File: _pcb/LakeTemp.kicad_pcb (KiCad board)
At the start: 2 copper layers, 98 x 70 mm, 50 parts, among them J1 Conn_01x06_Male, J2 Conn_01x03_Male, J3 Conn_01x02_Female, J4 Conn_01x14_Female, J5 Conn_01x04_Male, J6 Conn_01x06_Male, J7 Conn_01x02_Female, J8 Conn_01x03_Female, J9 Conn_01x02_Female, Q1 S8050, SW1 RESET, SW2 FLASH, U1 PCF8574, U2 ICL7660, U3 NCP1117-3.3_SOT223, U4 ESP-12E, U5 DS18B20

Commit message: Update PCB
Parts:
- removed ADR-A0: SolderJumper_2_Open, Jumper:SolderJumper-2_P1.3mm_Open_TrianglePad1.0x1.5mm
- added ADR-A3: SolderJumper_2_Open, Jumper:SolderJumper-2_P1.3mm_Open_TrianglePad1.0x1.5mm, F.Cu at (188.1, 84.2)
- added C6: 1000uF, Capacitor_SMD:CP_Elec_10x10.5, F.Cu at (154.5, 90.0)
- added D4: PWR 3.3V, LED_SMD:LED_0805_2012Metric_Pad1.15x1.40mm_HandSolder, F.Cu at (181.0, 111.3)
- added D5: WS2812B, LED_SMD:LED_WS2812B_PLCC4_5.0x5.0mm_P3.2mm, B.Cu at (120.6, 55.2)
- added J10: Conn_01x03_Male, Connector_JST:JST_PH_B3B-PH-K_1x03_P2.00mm_Vertical, F.Cu at (114.0, 67.0)
- added JP2: SolderJumper_3_Open, Connector_PinHeader_2.54mm:PinHeader_1x03_P2.54mm_Vertical, F.Cu at (113.5, 81.5)
- added R15: 4,7k, Resistor_SMD:R_0805_2012Metric_Pad1.20x1.40mm_HandSolder, F.Cu at (127.5, 74.8)
- added R16: 10k, Resistor_SMD:R_0805_2012Metric_Pad1.20x1.40mm_HandSolder, F.Cu at (127.6, 65.7)
- C1, C2, C3, C4: value 10uF 50V -> 10uF
- D1: value WS2812B -> PWR 5V; footprint LED_SMD:LED_WS2812B_PLCC4_5.0x5.0mm_P3.2mm -> LED_SMD:LED_0805_2012Metric_Pad1.15x1.40mm_HandSolder; moved to F.Cu
- D2: value LED -> PWR 3.3V
- D3: value LED -> PWR 5V
- J1: value Conn_01x06_Male -> Conn_01x02_Female; footprint Connector_JST:JST_PH_S6B-PH-K_1x06_P2.00mm_Horizontal -> TerminalBlock_Phoenix:TerminalBlock_Phoenix_MKDS-1,5-2-5.08_1x02_P5.08mm_Horizontal
- J2: value Conn_01x03_Male -> Conn_01x06_Male; footprint Connector_JST:JST_PH_B3B-PH-K_1x03_P2.00mm_Vertical -> Connector_JST:JST_PH_S6B-PH-K_1x06_P2.00mm_Horizontal
- J3: value Conn_01x02_Female -> Conn_01x06_Male; footprint Connector_JST:JST_PH_B2B-PH-K_1x02_P2.00mm_Vertical -> Connector_JST:JST_PH_B6B-PH-K_1x06_P2.00mm_Vertical
- J4: value Conn_01x14_Female -> Conn_01x03_Female; footprint Connector_PinHeader_2.54mm:PinHeader_1x14_P2.54mm_Vertical -> TerminalBlock_Phoenix:TerminalBlock_Phoenix_MKDS-1,5-3-5.08_1x03_P5.08mm_Horizontal; moved to F.Cu
- J5: value Conn_01x04_Male -> Conn_01x02_Female; footprint Connector_PinHeader_2.54mm:PinHeader_1x04_P2.54mm_Vertical -> TerminalBlock_Phoenix:TerminalBlock_Phoenix_MKDS-1,5-2-5.08_1x02_P5.08mm_Horizontal
- J6: value Conn_01x06_Male -> Conn_01x02_Female; footprint Connector_JST:JST_PH_B6B-PH-K_1x06_P2.00mm_Vertical -> Connector_JST:JST_PH_B2B-PH-K_1x02_P2.00mm_Vertical
- J7: value Conn_01x02_Female -> Conn_01x04_Male; footprint TerminalBlock_Phoenix:TerminalBlock_Phoenix_MKDS-1,5-2-5.08_1x02_P5.08mm_Horizontal -> Connector_PinHeader_2.54mm:PinHeader_1x04_P2.54mm_Vertical
- J8: value Conn_01x03_Female -> Conn_01x14_Female; footprint TerminalBlock_Phoenix:TerminalBlock_Phoenix_MKDS-1,5-3-5.08_1x03_P5.08mm_Horizontal -> Connector_PinHeader_2.54mm:PinHeader_1x14_P2.54mm_Vertical; moved to B.Cu
- J9: value Conn_01x02_Female -> Conn_01x04_Female; footprint TerminalBlock_Phoenix:TerminalBlock_Phoenix_MKDS-1,5-2-5.08_1x02_P5.08mm_Horizontal -> Connector_PinSocket_2.54mm:PinSocket_1x04_P2.54mm_Vertical
- JP1: footprint Jumper:SolderJumper-3_P2.0mm_Open_TrianglePad1.0x1.5mm -> Jumper:SolderJumper-3_P1.3mm_Bridged12_Pad1.0x1.5mm
- Q1: footprint Package_TO_SOT_SMD:SOT-23_Handsoldering -> Package_TO_SOT_THT:TO-92_Inline
- R1, R3: value 4,7k -> 150
- R11: value R_PHOTO -> 4,7k; footprint OptoDevice:R_LDR_5.1x4.3mm_P3.4mm_Vertical -> Resistor_SMD:R_0805_2012Metric_Pad1.20x1.40mm_HandSolder; moved to F.Cu
- R12: value R -> 10k
- R13: value R -> 4,7k
- R14: value R -> GL5528; footprint Resistor_SMD:R_0805_2012Metric_Pad1.20x1.40mm_HandSolder -> OptoDevice:R_LDR_5.1x4.3mm_P3.4mm_Vertical; moved to B.Cu
- R2, R4: value 4,7k -> 68
- R8: value 10k -> 4,7k
- SW1, SW2: footprint Button_Switch_SMD:SW_Push_1P1T_NO_6x6mm_H9.5mm -> Button_Switch_THT:SW_PUSH_6mm_H5mm
- U1: value PCF8574 -> NCP1117-3.3_SOT223; footprint Package_SO:SO-16_5.3x10.2mm_P1.27mm -> Package_TO_SOT_SMD:SOT-223-3_TabPin2
- U3: value NCP1117-3.3_SOT223 -> PCF8574; footprint Package_TO_SOT_SMD:SOT-223-3_TabPin2 -> Package_SO:SO-16_5.3x10.2mm_P1.27mm
- moved R14 93.3 mm to (110.5, 55.1)
- moved J9 82.9 mm to (124.1, 96.8), turned to 180 degrees
- moved C4 81.5 mm to (193.0, 68.2), turned to 180 degrees
- moved J8 81.1 mm to (194.5, 61.8), turned to 90 degrees
- moved C3 79.1 mm to (193.0, 66.0)
- moved J6 78.0 mm to (114.0, 76.0), turned to 90 degrees
- moved R13 67.1 mm to (127.5, 72.5), turned to 180 degrees
- moved J7 63.9 mm to (135.7, 84.3), turned to 90 degrees
- moved R11 58.9 mm to (176.5, 86.5)
- moved J4 58.7 mm to (162.4, 124.5), turned to 0 degrees
- moved R3 55.8 mm to (181.1, 106.7)
- moved R8 47.6 mm to (151.3, 68.0), turned to 180 degrees
- moved J2 47.2 mm to (165.0, 94.1), turned to 0 degrees
- moved J3 47.0 mm to (162.5, 109.3), turned to 0 degrees
- moved SW2 46.9 mm to (171.3, 66.7), turned to 270 degrees
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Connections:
- ADR-A1 pad 1: PCF_A1 -> PCF_A0
- ADR-A2 pad 1: PCF_A2 -> PCF_A1
- C1 pad 1: GND -> +5V
- C1 pad 2: Net-(C1-Pad2) -> GND
- C2 pad 1: Net-(C2-Pad1) -> +3V3
- C2 pad 2: Net-(C2-Pad2) -> GND
- C3 pad 1: +5V -> Net-(C3-Pad1)
- C3 pad 2: GND -> Net-(C3-Pad2)
- C4 pad 1: +3V3 -> Net-(C4-Pad1)
- D1 pad 1: +5V -> GND
- D1 pad 2: (no net) -> Net-(D1-Pad2)
- J1 pad 2: +5V -> Net-(J1-Pad2)
- J2 pad 2: +3V3 -> +5V
- J2 pad 3: TOUCH_IO -> +3V3
- J3 pad 1: +5V -> GND
- J3 pad 2: Net-(J3-Pad2) -> Net-(J1-Pad2)
- J4 pad 1: GND -> Net-(J3-Pad4)
- J4 pad 2: +5V -> Net-(J3-Pad5)
- J4 pad 3: LCD_CONTRAST -> GND
- J5 pad 1: ESP_TX -> Net-(J3-Pad3)
- J5 pad 2: ESP_RX -> Net-(J3-Pad6)
- J6 pad 1: Net-(J6-Pad1) -> +5V
- J7 pad 1: Net-(J6-Pad1) -> ESP_TX
- J7 pad 2: Net-(J6-Pad2) -> ESP_RX
- J8 pad 1: Net-(J6-Pad4) -> GND
- J8 pad 2: Net-(J6-Pad5) -> +5V
- J8 pad 3: GND -> LCD_CONTRAST
- J9 pad 1: Net-(J6-Pad3) -> +3V3
- J9 pad 2: Net-(J6-Pad6) -> GND
- Q1 pad 3: Net-(J3-Pad2) -> Net-(JP2-Pad3)
- R1 pad 1: +3V3 -> +5V
- R1 pad 2: SDA -> Net-(D1-Pad2)
- R11 pad 1: +3V3 -> ONEWIRE_PWR
- R11 pad 2: LDR -> ONEWIRE_BUS
- R12 pad 1: LDR -> GND
- R12 pad 2: GND -> Net-(R12-Pad2)
- R13 pad 1: Net-(J6-Pad2) -> WATER_LEVEL
- R13 pad 2: Net-(D2-Pad2) -> GND
- R14 pad 1: Net-(J6-Pad3) -> +3V3
- R14 pad 2: Net-(D3-Pad2) -> LDR
- R2 pad 2: SCL -> Net-(D2-Pad2)
- R3 pad 1: +5V -> Net-(J1-Pad2)
- R3 pad 2: LCD_LED -> Net-(D3-Pad2)
- R4 pad 1: +3V3 -> Net-(J3-Pad3)
- R4 pad 2: ONEWIRE_BUS -> Net-(D4-Pad2)
- R8 pad 1: GND -> +3V3
- R8 pad 2: Net-(R8-Pad2) -> SDA
- R9 pad 1: WATER_LEVEL -> +3V3
- R9 pad 2: GND -> SCL
- RV1 pad 1: Net-(C1-Pad2) -> Net-(C4-Pad1)
- U1 pad 1: PCF_A0 -> GND
- U1 pad 2: PCF_A1 -> +3V3
- U1 pad 3: PCF_A2 -> +5V
- U2 pad 1: (no net) -> Net-(U2-Pad1)
- U2 pad 2: Net-(C2-Pad1) -> Net-(C3-Pad1)
- U2 pad 4: Net-(C2-Pad2) -> Net-(C3-Pad2)
- U2 pad 5: Net-(C1-Pad2) -> Net-(C4-Pad1)
- U2 pad 6: (no net) -> Net-(U2-Pad6)
- U2 pad 7: (no net) -> Net-(U2-Pad7)
- U3 pad 1: GND -> PCF_A0
- U3 pad 2: +3V3 -> PCF_A1
- U3 pad 3: +5V -> PCF_A2
- U4 pad 10: (no net) -> Net-(U4-Pad10)
- U4 pad 11: (no net) -> Net-(U4-Pad11)
- U4 pad 12: (no net) -> Net-(U4-Pad12)
- U4 pad 13: (no net) -> Net-(U4-Pad13)
- U4 pad 14: (no net) -> Net-(U4-Pad14)
- U4 pad 16: Net-(R8-Pad2) -> Net-(R12-Pad2)
- U4 pad 9: (no net) -> Net-(U4-Pad9)
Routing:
- net Net-(J3-Pad3): track 0.00 -> 42.8 mm
- net Net-(J1-Pad2): track 0.00 -> 34.8 mm
- net Net-(J3-Pad6): track 0.00 -> 22.3 mm
- net Net-(J3-Pad4): track 0.00 -> 17.7 mm
- net Net-(J3-Pad5): track 0.00 -> 16.5 mm
- net Net-(D3-Pad2): track 0.00 -> 2.29 mm
- net Net-(D4-Pad2): track 0.00 -> 2.29 mm
- net GND: vias 0 -> 1
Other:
- board size 98 x 70 mm -> 90 x 82 mm
- board text added: "1W+"
- board text added: "1WD"
- board text added: "3.3V"
- board text added: "3.3V 1W PWR 5V"
- board text added: "3.3V OK"
- board text added: "5V"
- board text added: "5V OK"
- board text added: "ADR1"
- board text added: "ADR2"
- board text added: "ADR3"
- board text added: "BME280"
- board text added: "CONNECTOR PCB"
- board text added: "DATA"
- board text added: "ESP TXD/RXD"
- board text added: "FIX | Q1 LED PWR"
- board text added: "FLASH"
- board text added: "GND"
- board text added: "IO"
- board text added: "JLCJLCJLCJLC"
- board text added: "LCD LED"
- board text added: "MAIN PCB"
- board text added: "ONEWIRE"
- board text added: "PWR IN"
- board text added: "RESET"
- board text added: "RX"
- board text added: "STATUS"
- board text added: "TOUCH BTN"
- board text added: "TX"
- board text added: "VCC"
- board text added: "WATER LVL"
- board text added: "WTR"

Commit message: Finished PCB v1.0
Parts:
- added REF**: KiCad-Logo2_5mm_SilkScreen, Symbol:KiCad-Logo2_5mm_SilkScreen, B.Cu at (173.3, 78.3)
- added REF**: KiCad-Logo2_5mm_SilkScreen, Symbol:KiCad-Logo2_5mm_SilkScreen, B.Cu at (167.3, 115.3)
- moved C3 3.18 mm to (193.0, 69.2)
- moved C2 2.75 mm to (176.5, 84.2)
- moved C1 2.00 mm to (176.5, 82.0)
- moved J7 1.89 mm to (135.7, 86.2)
- moved D1 1.78 mm to (138.7, 94.8)
- moved D2 1.78 mm to (138.8, 97.3)
- moved R1 1.78 mm to (142.8, 94.8)
- moved R2 1.78 mm to (142.8, 97.3)
- moved C4 1.61 mm to (193.0, 66.6), turned to 0 degrees
- moved R9 0.90 mm to (151.4, 64.8)
- moved R16 0.89 mm to (127.6, 64.8)
- moved U1 0.69 mm to (169.3, 84.2), turned to 180 degrees
- moved R5 0.63 mm to (127.6, 67.4)
- moved R8 0.62 mm to (151.4, 67.4)
- moved R3 0.51 mm to (181.1, 106.2)
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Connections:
- D3 pad 1: GND -> GND1
- D4 pad 1: GND -> GND1
- J1 pad 1: GND -> GND1
- J3 pad 1: GND -> GND1
- J4 pad 3: GND -> GND1
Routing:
- net +3V3: track 0.00 -> 219.5 mm, vias 0 -> 1
- net +5V: track 0.00 -> 190.7 mm, vias 0 -> 6
- net SCL: track 0.00 -> 82.3 mm, vias 0 -> 4
- net SDA: track 0.00 -> 78.6 mm, vias 0 -> 6
- net ONEWIRE_BUS: track 0.00 -> 75.5 mm, vias 0 -> 4
- net LCD_LED: track 0.00 -> 71.2 mm, vias 0 -> 4
- net WATER_LEVEL: track 0.00 -> 69.1 mm, vias 0 -> 2
- net Net-(R5-Pad1): track 0.00 -> 46.9 mm, vias 0 -> 2
- net Net-(R7-Pad1): track 0.00 -> 39.9 mm, vias 0 -> 1
- net ONEWIRE_PWR: track 0.00 -> 34.6 mm
- net ESP_TX: track 0.00 -> 30.2 mm, vias 0 -> 1
- net ESP_RX: track 0.00 -> 27.5 mm, vias 0 -> 1
- net LCD_CONTRAST: track 0.00 -> 26.8 mm
- net TOUCH_IO: track 0.00 -> 25.4 mm, vias 0 -> 2
- net WS2812B: track 0.00 -> 25.1 mm, vias 0 -> 1
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- added copper zone on B.Cu, net GND1
- added copper zone on F.Cu, net GND1
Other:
- board text added: "Connector PCB"
- board text added: "LakeTempESP"
- board text added: "Main PCB"
- board text added: "REV 1.0 2021/05"
- board text added: "https://github.com/foorschtbar/LakeTempESP"

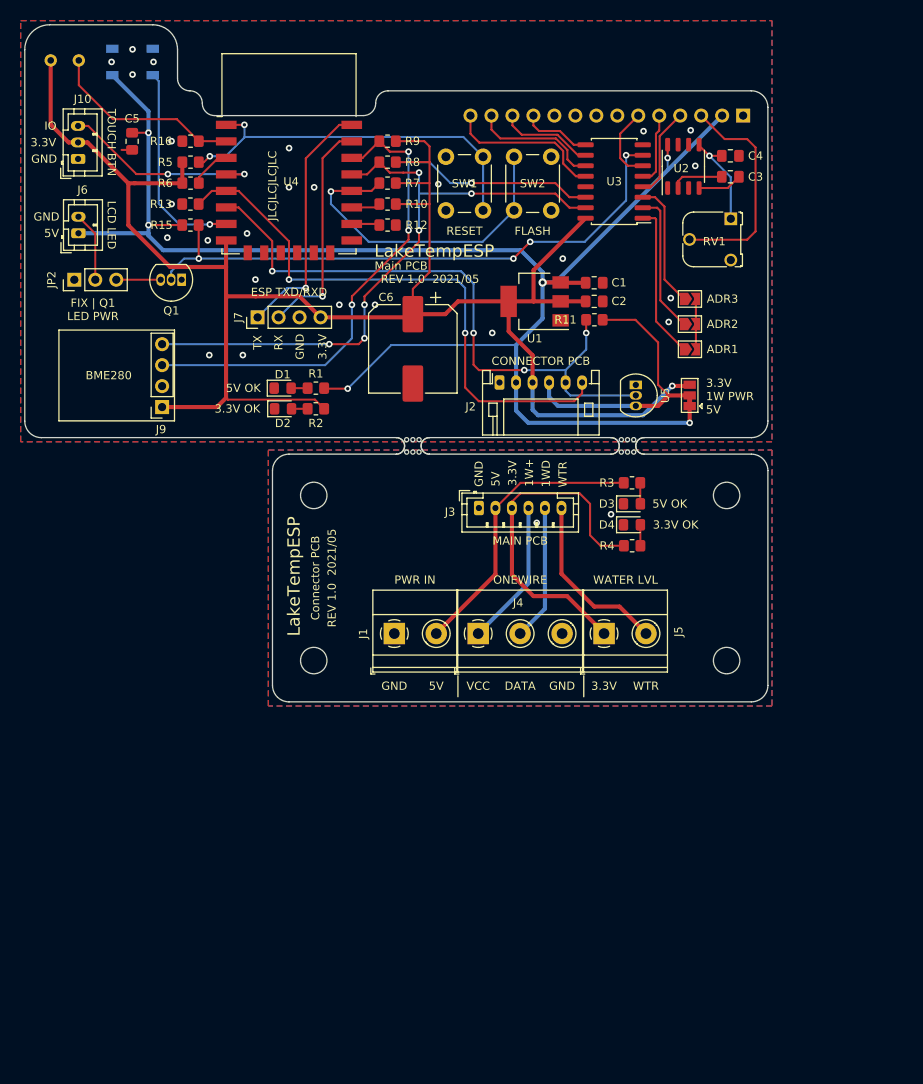
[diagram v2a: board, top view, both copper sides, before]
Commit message: Updated PCB to REV 2.0
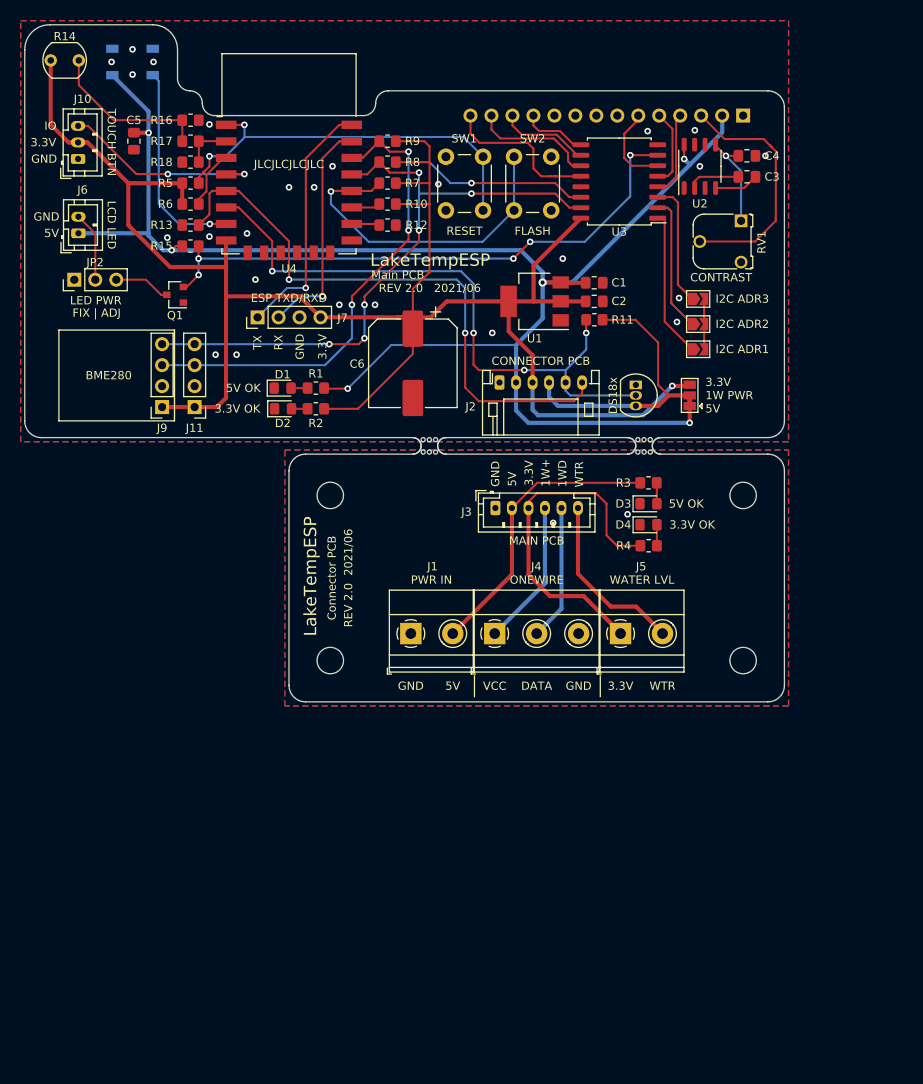
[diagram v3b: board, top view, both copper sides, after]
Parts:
- removed the REF** at (142.5, 107.8)
- removed the REF** at (142.5, 127.8)
- removed the REF** at (192.5, 127.8)
- removed the REF** at (192.5, 107.8)
- removed the mouse-bite-2mm-slot at (180.5, 101.8)
- removed the mouse-bite-2mm-slot at (154.5, 101.8)
- added J11: Conn_01x04_Female, Connector_PinHeader_2.54mm:PinHeader_1x04_P2.54mm_Vertical, F.Cu at (128.1, 97.1)
- added R17: 220K, Resistor_SMD:R_0805_2012Metric_Pad1.20x1.40mm_HandSolder, F.Cu at (127.6, 64.8)
- added R18: 100K, Resistor_SMD:R_0805_2012Metric_Pad1.20x1.40mm_HandSolder, F.Cu at (127.6, 67.4)
- added REF**: MountingHole_3.2mm_M3, MountingHole:MountingHole_3.2mm_M3, F.Cu at (144.5, 107.8)
- added REF**: MountingHole_3.2mm_M3, MountingHole:MountingHole_3.2mm_M3, F.Cu at (144.5, 127.8)
- added REF**: MountingHole_3.2mm_M3, MountingHole:MountingHole_3.2mm_M3, F.Cu at (194.5, 127.8)
- added REF**: MountingHole_3.2mm_M3, MountingHole:MountingHole_3.2mm_M3, F.Cu at (194.5, 107.8)
- added mouse-bite-2mm-slot: VAL**, foorschtbar:mouse-bite-2mm-slot, F.Cu at (182.5, 101.8)
- added mouse-bite-2mm-slot: VAL**, foorschtbar:mouse-bite-2mm-slot, F.Cu at (156.5, 101.8)
- Q1: footprint Package_TO_SOT_THT:TO-92_Inline -> Package_TO_SOT_SMD:SOT-23
- R10, R12, R16, R5, R6, R7: value 10k -> 10K
- R11, R13, R15, R8, R9: value 4,7k -> 4,7K
- R14: moved to F.Cu
- RV1: value R_POT_TRIM -> 10K
- U3: footprint Package_SO:SO-16_5.3x10.2mm_P1.27mm -> Package_SO:SOIC-16W_7.5x10.3mm_P1.27mm
- moved REF** 2.77 mm to (169.6, 113.8)
- moved R13 2.54 mm to (127.6, 75.0)
- moved R15 2.54 mm to (127.6, 77.5)
- moved R16 2.54 mm to (127.6, 62.3), turned to 0 degrees
- moved R5 2.54 mm to (127.6, 69.9)
- moved R6 2.54 mm to (127.6, 72.5)
- moved REF** 2.01 mm to (172.2, 80.0)
- moved C3 2.00 mm to (195.0, 69.2)
- moved C4 2.00 mm to (195.0, 66.6)
- moved D3 2.00 mm to (183.0, 108.8)
- moved D4 2.00 mm to (183.0, 111.3)
- moved J1 2.00 mm to (154.3, 124.5)
- moved J3 2.00 mm to (164.5, 109.3)
- moved J4 2.00 mm to (164.4, 124.5)
- moved J5 2.00 mm to (179.7, 124.5)
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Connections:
- U4 pad 2: LDR -> Net-(R17-Pad1)
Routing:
- net +3V3: track 219.5 -> 225.4 mm
- net Net-(R17-Pad1): track 0.00 -> 5.87 mm
- net LDR: track 23.7 -> 20.1 mm
- net LCD_CONTRAST: track 26.8 -> 30.1 mm
- net Net-(R6-Pad1): track 5.00 -> 8.13 mm
- net WATER_LEVEL: track 69.1 -> 72.1 mm
- net PCF_A0: track 19.8 -> 17.3 mm
- net Net-(R5-Pad1): track 46.9 -> 49.4 mm
- net SCL: track 82.3 -> 80.8 mm
- net Net-(JP2-Pad3): track 5.38 -> 6.87 mm
- net LCD_DB4: track 8.48 -> 7.05 mm
- net LCD_LED: track 71.2 -> 69.8 mm, vias 4 -> 5
- net +5V: track 190.7 -> 189.3 mm
- net LCD_E: track 9.18 -> 10.5 mm
- net GND: track 8.13 -> 6.86 mm
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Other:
- board size 90 x 82 mm -> 92 x 82 mm
- rule pad_to_mask_clearance: 0.05 -> 0
- board text added: "(c) 2021 foorschtbar"
- board text added: "CONTRAST"
- board text added: "DS18x"
- board text added: "FIX | ADJ"
- board text added: "I2C ADR1"
- board text added: "I2C ADR2"
- board text added: "I2C ADR3"
- board text added: "LED PWR"
- board text added: "REV 2.0 2021/06"
- board text added: "github.com/foorschtbar/LakeTempESP"
- board text removed: "ADR1"
- board text removed: "ADR2"
- board text removed: "ADR3"
- board text removed: "FIX | Q1 LED PWR"
- board text removed: "REV 1.0 2021/05"
- board text removed: "https://github.com/foorschtbar/LakeTempESP"

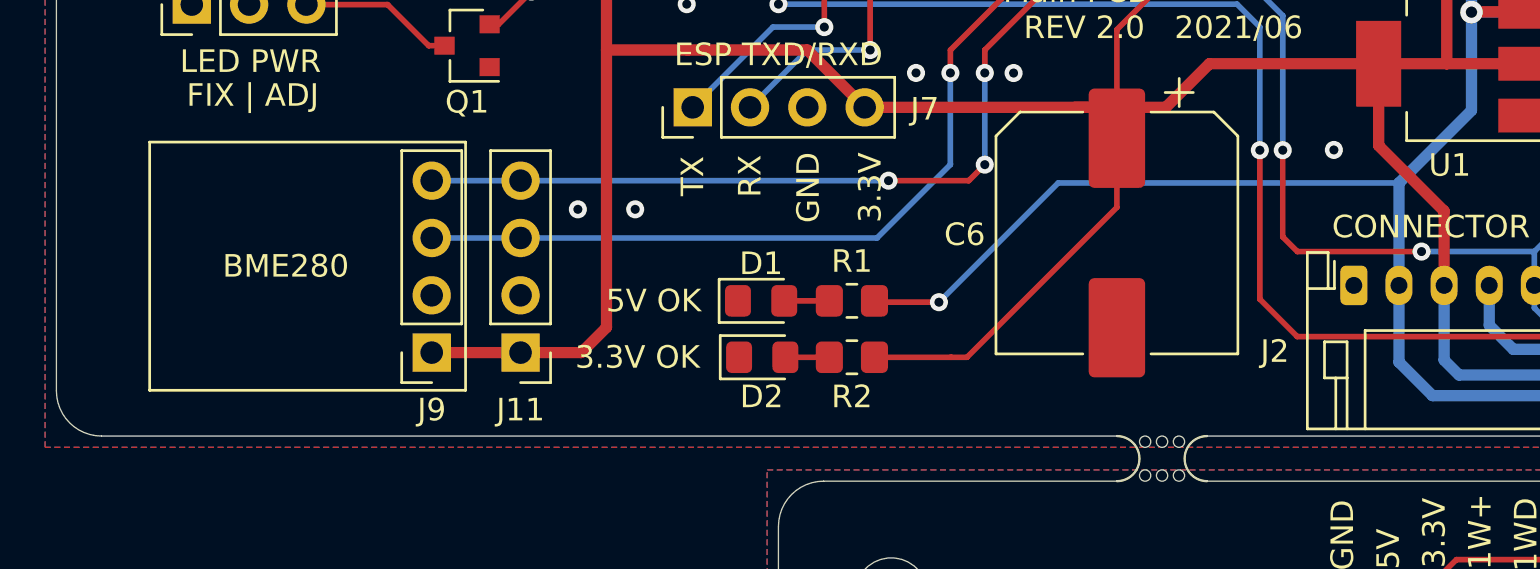
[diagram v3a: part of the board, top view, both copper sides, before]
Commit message: Added Labels to Aux I2C Connector
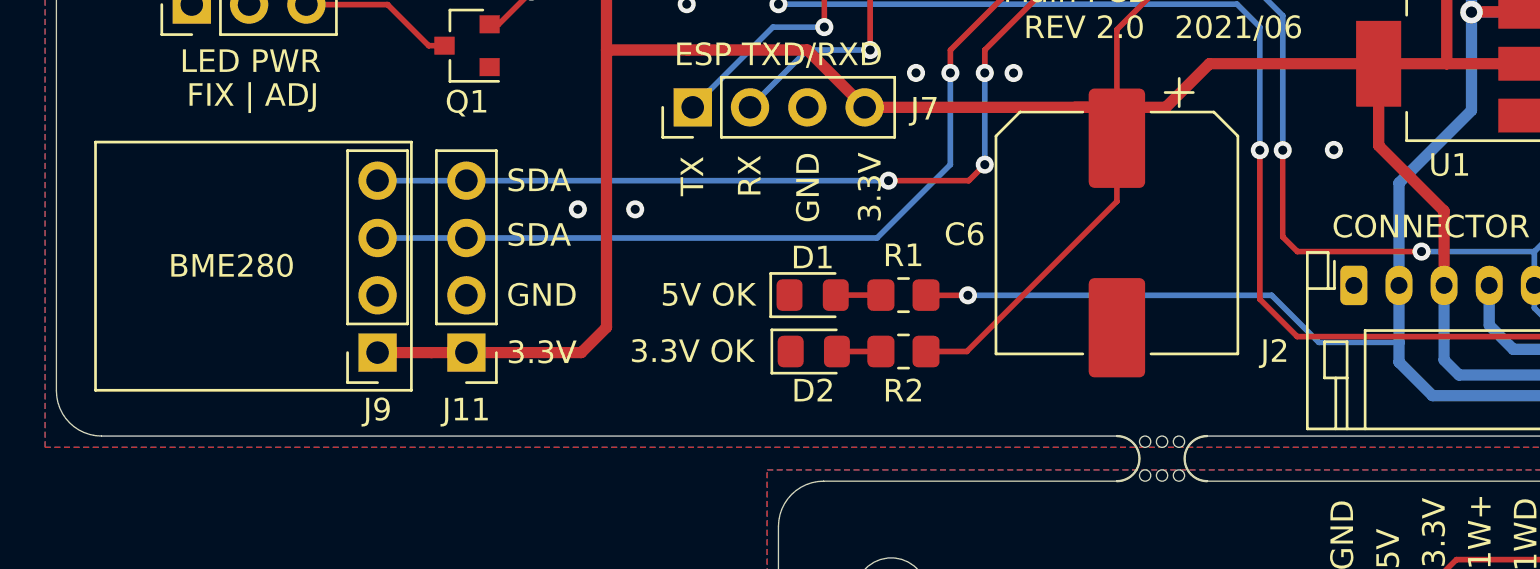
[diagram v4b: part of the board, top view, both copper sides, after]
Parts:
- moved J11 2.40 mm to (125.7, 97.1)
- moved J9 2.40 mm to (121.7, 97.1)
- moved D1 2.30 mm to (141.0, 94.5)
- moved D2 2.30 mm to (141.1, 97.0)
- moved R1 2.30 mm to (145.1, 94.5)
- moved R2 2.30 mm to (145.1, 97.0)
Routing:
- net +5V: track 189.3 -> 185.8 mm
- net SDA: track 77.3 -> 79.7 mm
- net SCL: track 80.8 -> 83.2 mm
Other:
- board text added: "SDA"

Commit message: Updated README
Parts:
- ADR-A1, ADR-A2, ADR-A3: footprint Jumper:SolderJumper-2_P1.3mm_Open_TrianglePad1.0x1.5mm -> Jumper:SolderJumper-3_P1.3mm_Bridged12_RoundedPad1.0x1.5mm_NumberLabels
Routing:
- net +3V3: track 225.2 -> 236.6 mm
- net GND: track 6.86 -> 6.10 mm
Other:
- board text added: "ADR1"
- board text added: "ADR2"
- board text added: "ADR3"
- board text added: "REV 2.1 2021/06"
- board text removed: "I2C ADR1"
- board text removed: "I2C ADR2"
- board text removed: "I2C ADR3"
